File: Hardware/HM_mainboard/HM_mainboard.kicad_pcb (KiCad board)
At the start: 2 copper layers, 79.5 x 55 mm, 66 parts, among them J1 JST PH2P ST90, J2 USB4105-GF-A, J3 Conn_01x04, J4 54-00174, J5 009159005551906, J6 54-00174, J7 54-00174, J8 54-00174, Q1 PMOS AS3401, U1 MCP73831-2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

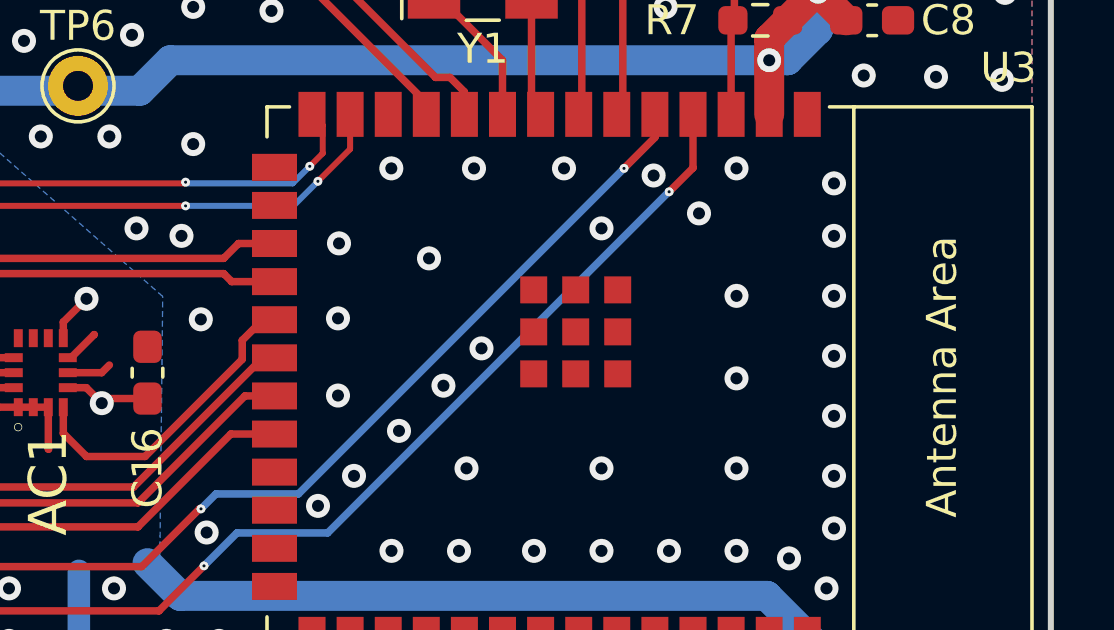
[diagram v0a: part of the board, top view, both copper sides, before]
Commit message: Added hardware version to PCB silkscreen
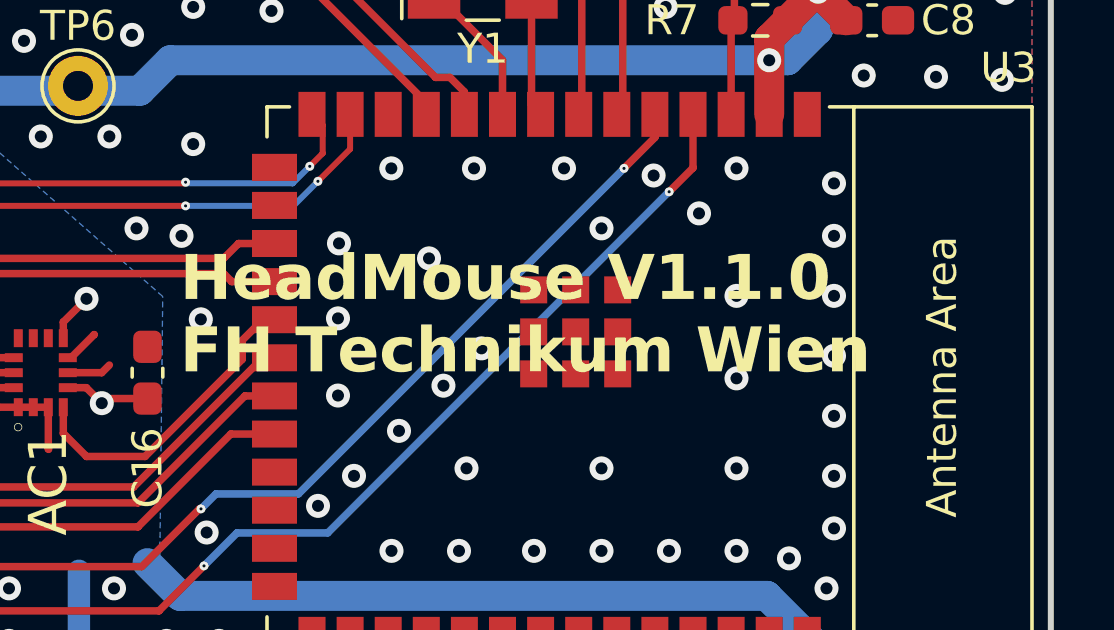
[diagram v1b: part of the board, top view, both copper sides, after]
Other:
- board text added: "HeadMouse V1.1.0 FH Technikum Wien"
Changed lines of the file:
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@@
     (effects (font (size 1.5 1.5) (thickness 0.3) bold) (justify left bottom mirror))
+  )
+  (gr_text "HeadMouse V1.1.0\nFH Technikum Wien" (at 167.2 99.2) (layer "F.SilkS")
+    (effects (font (size 1.5 1.5) (thickness 0.3) bold) (justify left bottom))
   )
   (segment (start 164.338 97.79) (end 164.338 97.79162) (width 0.25) (layer "F.Cu") (net 1))

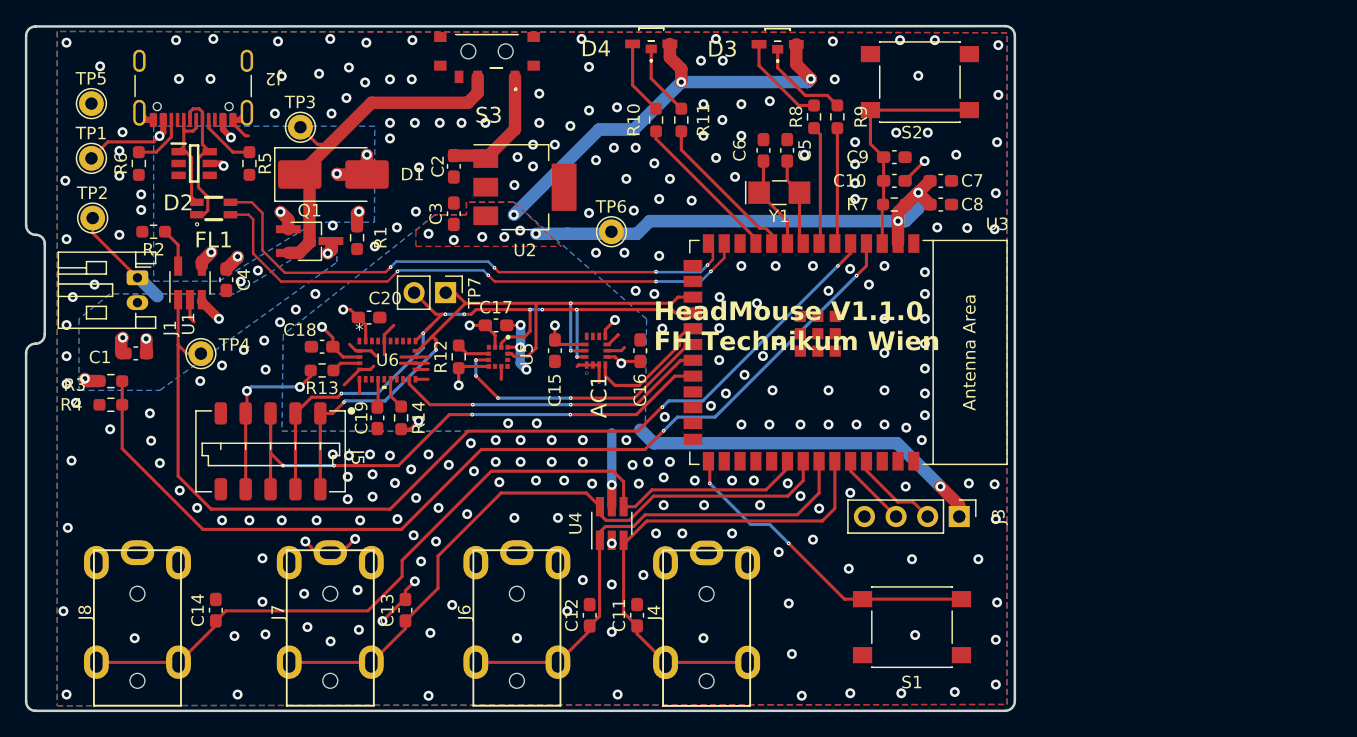
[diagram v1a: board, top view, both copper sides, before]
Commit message: Updated schematic and PCB according to Email from BA on 16th of April
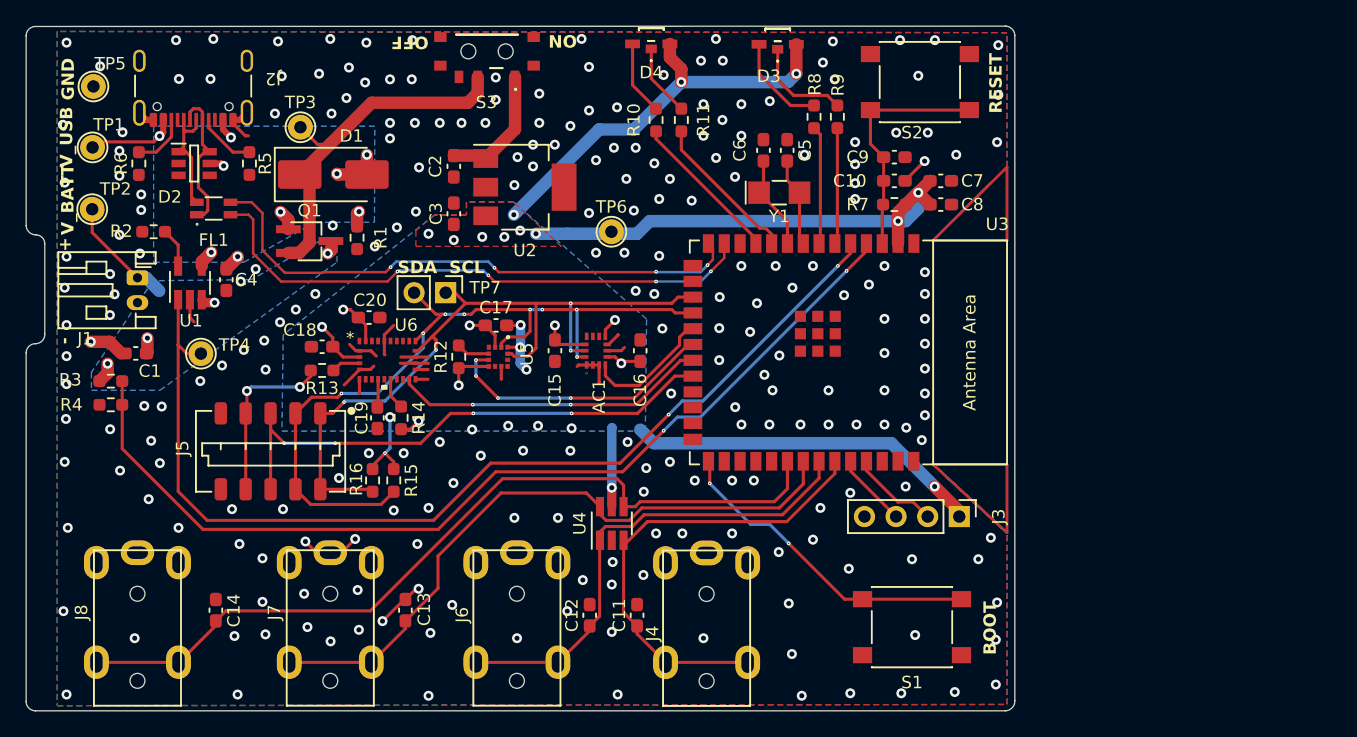
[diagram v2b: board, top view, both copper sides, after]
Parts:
- added LOGO2: Logo_KiCAD, Symbol:KiCad-Logo_5mm_SilkScreen, B.Cu at (186.8, 78.9)
- added LOGO3: Logo_CE, Symbol:CE-Logo_8.5x6mm_SilkScreen, B.Cu at (175.4, 93.4)
- added LOGO4: Logo_WEEE, Symbol:WEEE-Logo_5.6x8mm_SilkScreen, B.Cu at (187.2, 93.8)
- added R15: 4k7, Resistor_SMD:R_0603_1608Metric_Pad0.98x0.95mm_HandSolder, F.Cu at (146.3, 109.5)
- added R16: 4k7, Resistor_SMD:R_0603_1608Metric_Pad0.98x0.95mm_HandSolder, F.Cu at (144.6, 109.5)
- C10, C19, C2, C3: value 1.0uF-25V-(+80/-20%) -> 1.0uF
- R1: value 10k/1% -> 10k
- R3, R4: value 10k -> 100k
- TP6: value TestPoint_Probe -> 3v3
- moved TP5 1.39 mm to (122.2, 77.8)
- moved TP1 0.88 mm to (122.1, 82.7)
- moved TP2 0.71 mm to (122.1, 87.7)
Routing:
- net /I2C_SDA: track 56.2 -> 65.0 mm
- net 3.3V: track 150.4 -> 155.0 mm, vias 23 -> 25
- net /I2C_SCL: track 55.9 -> 60.2 mm
- net /MPRLS_INT: track 46.6 -> 44.0 mm
- net /BTN_1: track 39.5 -> 37.8 mm
- net /BATT_CHARGING_STATUS: track 80.8 -> 82.2 mm
- net GND: track 48.2 -> 49.3 mm, vias 272 -> 246
- net /BTN_2: track 39.9 -> 39.2 mm
- net /V_BATT_MEASURE: track 78.5 -> 77.8 mm
- net Net-(D3-K1): track 7.55 -> 8.10 mm
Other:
- board text added: "+"
- board text added: "-"
- board text added: "BOOT"
- board text added: "GND"
- board text added: "HeadMouse mainboard v1.1.0"
- board text added: "OFF"
- board text added: "ON"
- board text added: "RESET"
- board text added: "SDA SCL"
- board text added: "V_BATT"
- board text added: "V_USB"
- board text added: "Vanessa Prankl, 2024 https://github.com/vanessaPrankl/HeadMouse.git"
- board text removed: "HeadMouse V1.0 FH Technikum Wien"
- board text removed: "HeadMouse V1.1.0 FH Technikum Wien"

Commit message: Uniform text alignment
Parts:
- turned LOGO2 to 0 degrees
- turned LOGO3 to 0 degrees
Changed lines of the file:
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@@
   )
   (footprint "Symbol:CE-Logo_8.5x6mm_SilkScreen" (layer "B.Cu")
-    (at 175.43 93.38 180)
+    (at 175.43 93.38)
     (descr "CE marking")
     (tags "Logo CE certification")
@@
   )
   (footprint "Symbol:KiCad-Logo_5mm_SilkScreen" (layer "B.Cu")
-    (at 186.825698 78.857938 180)
+    (at 186.825698 78.857938)
     (descr "KiCad Logo")
     (tags "Logo KiCad")

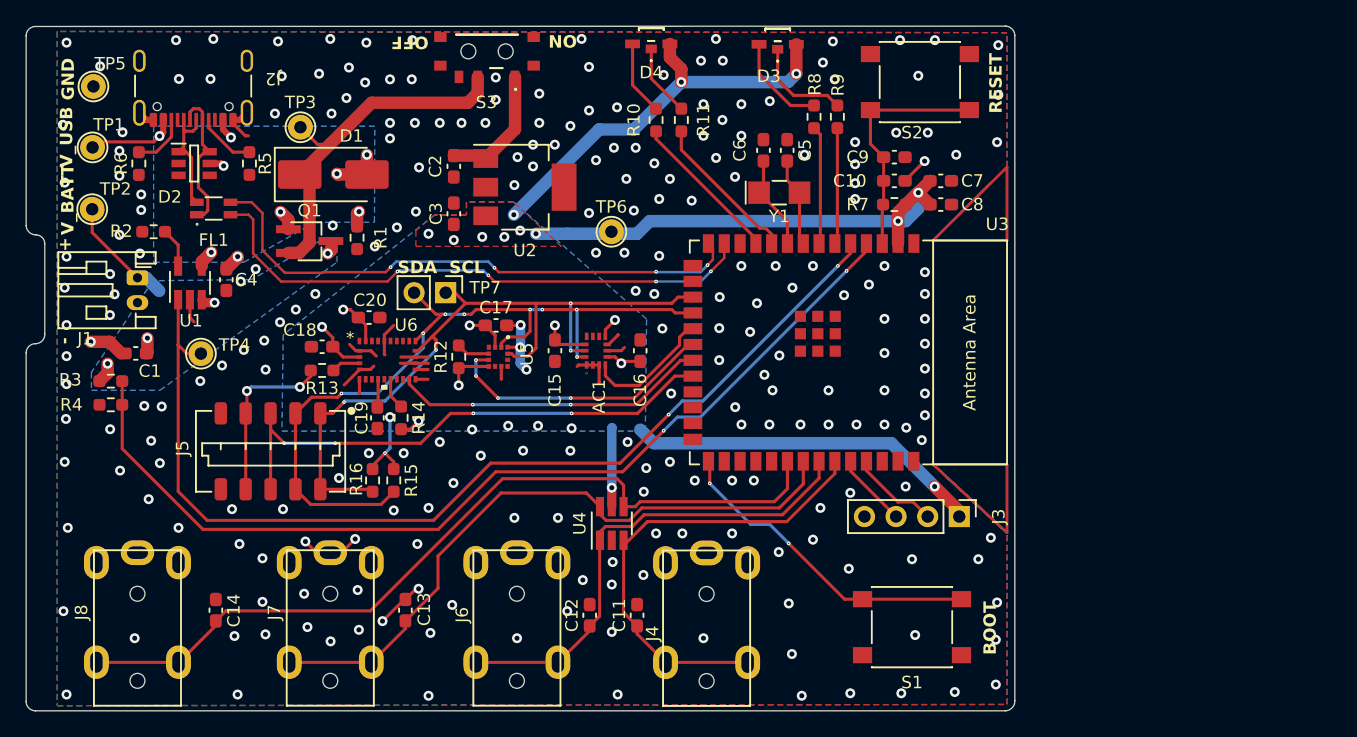
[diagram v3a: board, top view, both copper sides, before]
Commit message: Updated schematic to version v2.0.0
•	Removed two 6-Axis IMUs
•	As the BNO055 did not respond to I2C requests, a 2k7 pullup was added in parallel to the I2C-SDA pullup. The behavior is described here:  https://forums.adafruit.com/viewtopic.php?t=205215
•	Added mounting holes for enclosure
•	Added board description prints
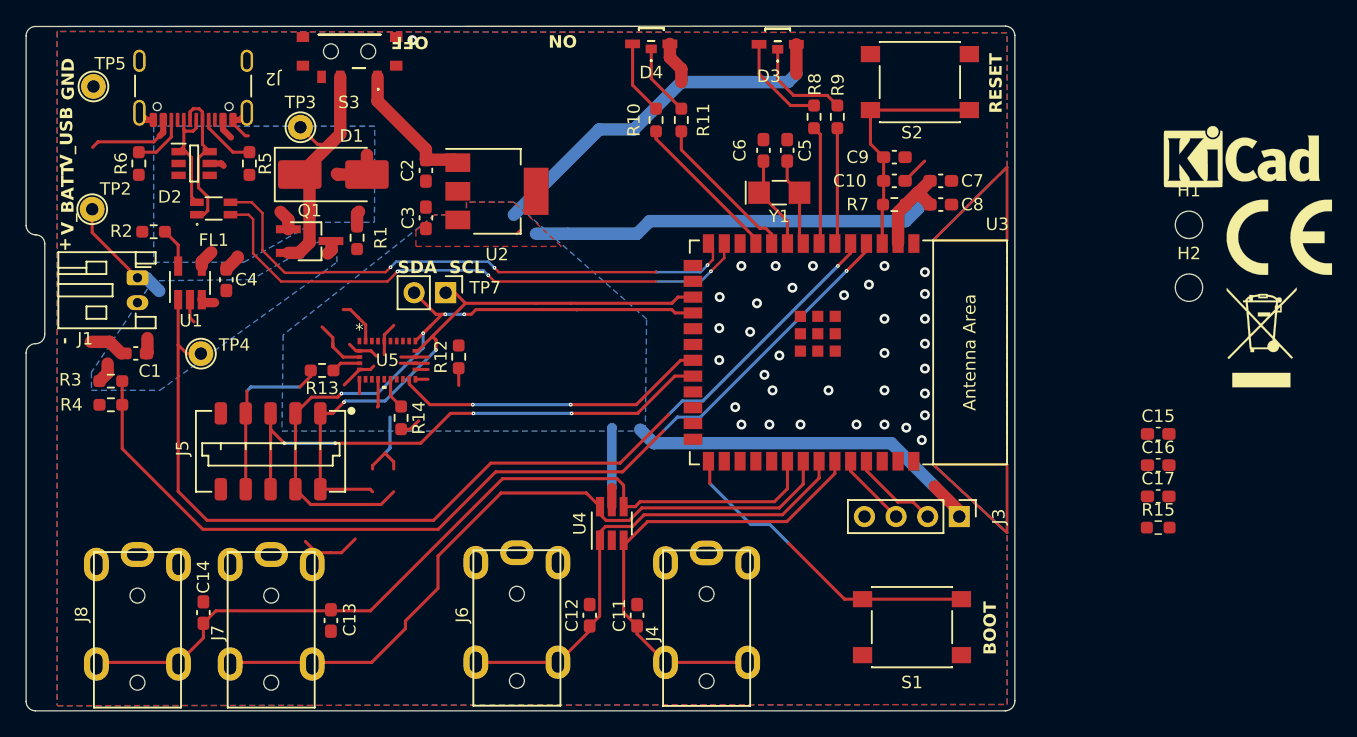
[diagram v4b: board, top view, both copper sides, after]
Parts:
- removed AC1: LSM6DSOXTR, HeadMouse:LSM6DSOXTR
- removed C18, C20: 100nF, Capacitor_SMD:C_0603_1608Metric_Pad1.08x0.95mm_HandSolder
- removed C19: 1.0uF, Capacitor_SMD:C_0603_1608Metric_Pad1.08x0.95mm_HandSolder
- removed R16: 4k7, Resistor_SMD:R_0603_1608Metric_Pad0.98x0.95mm_HandSolder
- removed TP1: TestPoint_Probe, TestPoint:TestPoint_THTPad_D2.0mm_Drill1.0mm
- removed TP6: 3v3, TestPoint:TestPoint_THTPad_D2.0mm_Drill1.0mm
- removed U6: BNO055, HeadMouse:QFN_BNO055_BOS
- added H1: MountingHole, MountingHole:MountingHole_2.2mm_M2_ISO7380, F.Cu at (210.2, 88.9)
- added H2: MountingHole, MountingHole:MountingHole_2.2mm_M2_ISO7380, F.Cu at (210.2, 94.0)
- added LOGO1: Logo_HM, HeadMouse:LOGO_HM_V2.0.0, F.Cu at (220.1, 94.2)
- C16: value 100nF -> 1.0uF
- LOGO2, LOGO3, LOGO4: moved to F.Cu
- R12, R13: value 10k -> 120
- R15: value 4k7 -> 10k
- R7: value 10k -> 4k7
- R8: value 120 -> 1k8
- R9: value 120 -> 10k
- U5: value MC6470 -> BNO055; footprint HeadMouse:PQFN50P200X200X100-12N -> HeadMouse:QFN_BNO055_BOS
- moved R15 61.6 mm to (207.8, 113.3), turned to 0 degrees
- moved C17 55.0 mm to (207.8, 110.8)
- moved C15 49.0 mm to (207.8, 105.8), turned to 0 degrees
- moved C16 42.6 mm to (207.8, 108.3), turned to 0 degrees
- moved LOGO3 42.2 mm to (217.5, 89.9)
- moved LOGO4 29.1 mm to (216.1, 98.0)
- moved LOGO2 28.1 mm to (214.5, 84.0)
- moved S3 11.1 mm to (142.8, 75.0)
- moved U5 8.91 mm to (145.8, 99.8), turned to 0 degrees
- moved C13 6.05 mm to (141.2, 120.8)
- moved J7 4.75 mm to (136.4, 127.8)
- moved C2 2.27 mm to (148.9, 84.6)
- moved C3 2.27 mm to (148.9, 88.4)
- moved U2 2.27 mm to (154.6, 86.2)
- moved C14 1.02 mm to (131.0, 120.1)
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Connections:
- net /BATT_CHARGING_STATUS renamed /BAT_CHRG_STATUS
- net /V_BATT_MEASURE renamed /V_BAT_MEASURE
- C16 pad 1: 3.3V -> GND
- C16 pad 2: GND -> Net-(U5-CAP)
- R10 pad 1: /LED_DEV_G -> /LED_BAT_G
- R10 pad 2: Net-(D4-K2) -> Net-(D3-K2)
- R11 pad 1: /LED_DEV_R -> /LED_BAT_R
- R11 pad 2: Net-(D4-K1) -> Net-(D3-K1)
- R12 pad 1: 3.3V -> /LED_STAT_G
- R12 pad 2: Net-(U5-INTA) -> Net-(D4-K2)
- R13 pad 1: Net-(U6-NBOOT_LOAD_PIN) -> /LED_STAT_R
- R13 pad 2: 3.3V -> Net-(D4-K1)
- R14 pad 1: Net-(U6-NRESET) -> Net-(U5-NBOOT_LOAD_PIN)
- R15 pad 1: /I2C_SDA -> Net-(U5-NRESET)
- R7 pad 1: /Microcontroller - ESP32-S3-WROOM/EN -> /I2C_SCL
- R8 pad 1: /LED_BAT_G -> /I2C_SDA
- R8 pad 2: Net-(D3-K2) -> 3.3V
- R9 pad 1: /LED_BAT_R -> /Microcontroller - ESP32-S3-WROOM/EN
- R9 pad 2: Net-(D3-K1) -> 3.3V
- U3 pad 10: /LED_DEV_R -> /LED_STAT_R
- U3 pad 11: /LED_DEV_G -> /LED_STAT_G
- U3 pad 12: /Microcontroller - ESP32-S3-WROOM/GPIO_8 -> unconnected-(U3-GPIO8/TOUCH8/ADC1_CH7/SUBSPICS1-Pad12)
- U3 pad 15: /Microcontroller - ESP32-S3-WROOM/GPIO_3 -> unconnected-(U3-GPIO3/TOUCH3/ADC1_CH2-Pad15)
- U3 pad 16: /Microcontroller - ESP32-S3-WROOM/GPIO_46 -> unconnected-(U3-GPIO46-Pad16)
- U3 pad 19: /LSM6DS_INT -> unconnected-(U3-GPIO11/TOUCH11/ADC2_CH0/FSPID/FSPIIO5/SUBSPID-Pad19)
- U3 pad 20: /MC6470_INT -> unconnected-(U3-GPIO12/TOUCH12/ADC2_CH1/FSPICLK/FSPIIO6/SUBSPICLK-Pad20)
- U3 pad 23: /Microcontroller - ESP32-S3-WROOM/GPIO_21 -> unconnected-(U3-GPIO21-Pad23)
- U3 pad 24: /Microcontroller - ESP32-S3-WROOM/GPIO_47 -> unconnected-(U3-GPIO47/SPICLK_P/SUBSPICLK_P_DIFF-Pad24)
- U3 pad 25: /Microcontroller - ESP32-S3-WROOM/GPIO_48 -> unconnected-(U3-GPIO48/SPICLK_N/SUBSPICLK_N_DIFF-Pad25)
- U3 pad 26: /Microcontroller - ESP32-S3-WROOM/GPIO_45 -> unconnected-(U3-GPIO45-Pad26)
- U3 pad 28: /Microcontroller - ESP32-S3-WROOM/GPIO_35 -> unconnected-(U3-SPIIO6/GPIO35/FSPID/SUBSPID-Pad28)
- U3 pad 29: /Microcontroller - ESP32-S3-WROOM/GPIO_36 -> unconnected-(U3-SPIIO7/GPIO36/FSPICLK/SUBSPICLK-Pad29)
- U3 pad 30: /Microcontroller - ESP32-S3-WROOM/GPIO_37 -> unconnected-(U3-SPIDQS/GPIO37/FSPIQ/SUBSPIQ-Pad30)
- U3 pad 31: /Microcontroller - ESP32-S3-WROOM/GPIO_38 -> unconnected-(U3-GPIO38/FSPIWP/SUBSPIWP-Pad31)
- U3 pad 38: /Microcontroller - ESP32-S3-WROOM/GPIO_2 -> unconnected-(U3-GPIO2/TOUCH2/ADC1_CH1-Pad38)
- U3 pad 39: /Microcontroller - ESP32-S3-WROOM/GPIO_1 -> unconnected-(U3-GPIO1/TOUCH1/ADC1_CH0-Pad39)
- U5 pad 1: GND -> unconnected-(U5-NC-Pad1)
- U5 pad 11: unconnected-(U5-NC-Pad11) -> Net-(U5-NRESET)
- U5 pad 12: /I2C_SCL -> unconnected-(U5-NC-Pad12)
- U5 pad 2: /I2C_SDA -> GND
- U5 pad 4: unconnected-(U5-NC-Pad4) -> Net-(U5-NBOOT_LOAD_PIN)
- U5 pad 5: Net-(U5-INTA) -> GND
- U5 pad 6: /MC6470_INT -> GND
- U5 pad 7: 3.3V -> unconnected-(U5-SWDIO-Pad7)
- U5 pad 9: GND -> Net-(U5-CAP)
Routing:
- net /MC6470_INT: track 22.3 -> 0.00 mm, vias 4 -> 0
- net 3.3V: track 155.0 -> 133.4 mm, vias 25 -> 0
- net GND: track 49.3 -> 32.5 mm, vias 246 -> 35
- net /LED_STAT_R: track 0.00 -> 14.7 mm
- net /LED_STAT_G: track 0.00 -> 13.9 mm
- net /LED_DEV_G: track 12.3 -> 0.00 mm
- net /LED_DEV_R: track 12.3 -> 0.00 mm
- net /I2C_SCL: track 60.2 -> 49.0 mm, vias 4 -> 2
- net /LSM6DS_INT: track 10.5 -> 0.00 mm
- net /I2C_SDA: track 65.0 -> 55.8 mm, vias 8 -> 4
- net /Battery_and_Power_Managment/V_PWR_SWITCH: track 29.4 -> 20.2 mm
- net Net-(D4-K1): track 5.81 -> 11.9 mm
- net /BTN_3: track 53.1 -> 58.0 mm
- net Net-(U5-INTA): track 2.68 -> 0.00 mm
- net Net-(U6-NRESET): track 2.54 -> 0.00 mm
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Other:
- board text removed: "HeadMouse mainboard v1.1.0"
- board text removed: "Vanessa Prankl, 2024 https://github.com/vanessaPrankl/HeadMouse.git"

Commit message: Added BOM, PDF and zipped V2.0.0 project data
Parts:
- removed J3: Conn_01x04, Connector_PinHeader_2.54mm:PinHeader_1x04_P2.54mm_Vertical
- removed J8: 54-00174, HeadMouse:54-00174
- removed TP3: TestPoint_Probe, TestPoint:TestPoint_THTPad_D2.0mm_Drill1.0mm
- removed TP7: TestPoint_2Pole, Connector_PinHeader_2.54mm:PinHeader_1x02_P2.54mm_Vertical
- added SW1: SKHHLQA010, Button_Switch_THT:SW_Tactile_SPST_Angled_PTS645Vx58-2LFS, F.Cu at (128.3, 125.2)
- LOGO2, LOGO3, LOGO4: moved to B.Cu
- moved H2 96.4 mm to (119.2, 125.6)
- moved LOGO4 78.8 mm to (137.6, 90.6), turned to 180 degrees
- moved C15 75.4 mm to (132.6, 99.8)
- moved C17 73.5 mm to (135.6, 96.8), turned to 90 degrees
- moved C16 71.3 mm to (136.6, 104.8), turned to 90 degrees
- moved R15 70.2 mm to (138.1, 104.8), turned to -90 degrees
- moved LOGO3 67.9 mm to (149.6, 90.6), turned to 180 degrees
- moved LOGO2 51.5 mm to (163.4, 90.4), turned to 180 degrees
- moved R7 44.8 mm to (143.0, 98.0), turned to 90 degrees
- moved H1 43.8 mm to (168.6, 75.2)
- moved R8 43.2 mm to (141.4, 99.4)
- moved TP5 40.0 mm to (120.4, 117.8)
- moved LOGO1 27.8 mm to (193.0, 88.2)
- moved U4 26.1 mm to (137.8, 110.8), turned to 180 degrees
- moved S2 26.0 mm to (162.6, 78.5), turned to -90 degrees
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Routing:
- net /BAT_CHRG_STATUS: track 82.2 -> 46.1 mm, vias 1 -> 2
- net /V_BAT_MEASURE: track 77.8 -> 43.0 mm, vias 1 -> 2
- net V_BATT: track 14.0 -> 38.7 mm, vias 0 -> 4
- net /BTN_4: track 67.1 -> 42.7 mm
- net GND: track 32.5 -> 8.72 mm, vias 35 -> 82
- net /I2C_SDA: track 55.8 -> 34.7 mm
- net V_USB: track 20.3 -> 40.7 mm, vias 0 -> 5
- net /Microcontroller - ESP32-S3-WROOM/USB_C_D-: track 46.2 -> 27.3 mm, vias 3 -> 0
- net /BTN_1: track 37.8 -> 55.7 mm
- net /BNO55_INT: track 25.3 -> 7.49 mm, vias 2 -> 0
- net /Microcontroller - ESP32-S3-WROOM/USB_C_D+: track 45.5 -> 27.8 mm, vias 3 -> 0
- net /I2C_SCL: track 49.0 -> 32.2 mm, vias 2 -> 4
- net /BTN_3: track 58.0 -> 41.9 mm, vias 0 -> 2
- net /MPRLS_INT: track 44.0 -> 30.5 mm, vias 4 -> 2
- net /LED_BAT_R: track 9.36 -> 20.9 mm, vias 0 -> 2
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- removed copper zone on B.Cu, net 3.3V
- removed copper zone on F.Cu, net 3.3V
- removed copper zone on B.Cu, net V_BATT
- removed copper zone on B.Cu, net V_USB
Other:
- board size 79.5 x 55 mm -> 54.2 x 55 mm
- board text added: "BAT"
- board text added: "BTN0"
- board text added: "BTN1"
- board text added: "BTN2"
- board text added: "BTN3"
- board text added: "CHRG_STAT"
- board text added: "STAT"
- board text removed: "SDA SCL"
- board text removed: "V_USB"
